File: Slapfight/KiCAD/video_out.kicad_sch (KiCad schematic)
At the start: 30 parts, among them U2_U11T_ 74LS32, U8R 74LS373

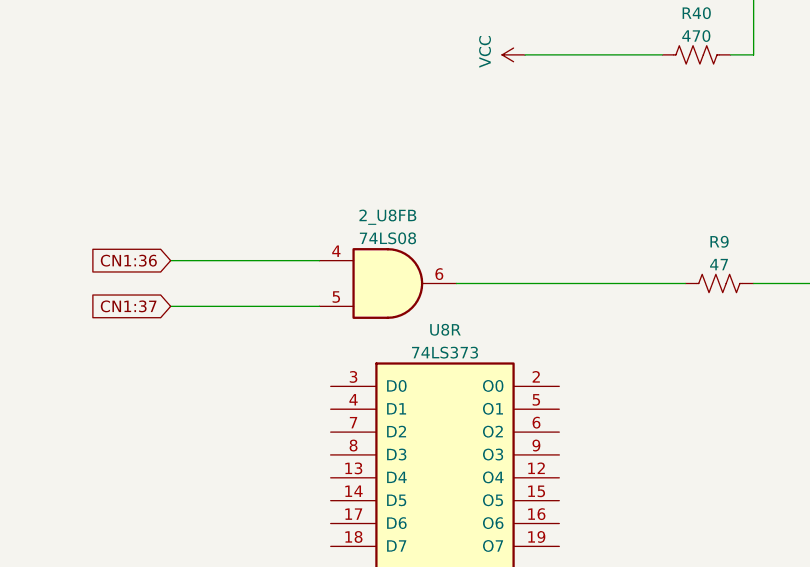
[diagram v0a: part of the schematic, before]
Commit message: Component naming updates
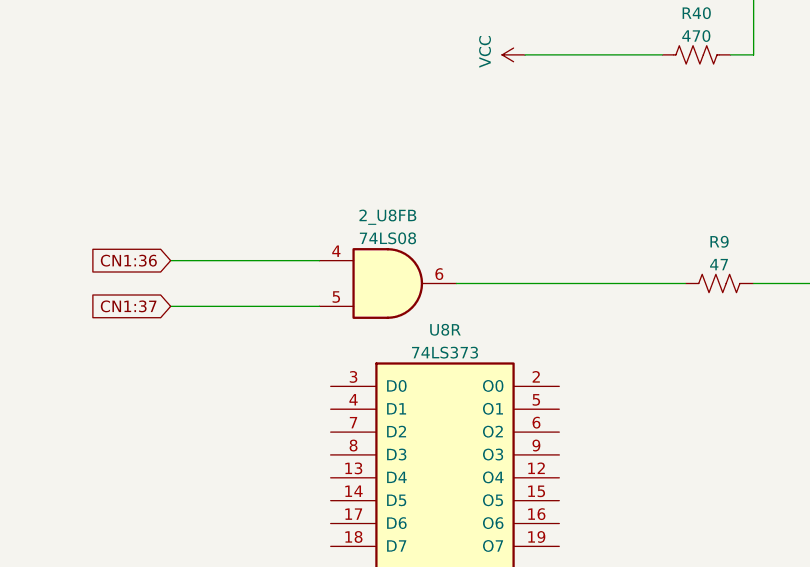
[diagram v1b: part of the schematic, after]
